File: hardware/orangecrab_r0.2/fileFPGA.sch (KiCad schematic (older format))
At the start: 11 parts, among them J6 JTAG, U3 ECP5U25, U6 AT25SF081

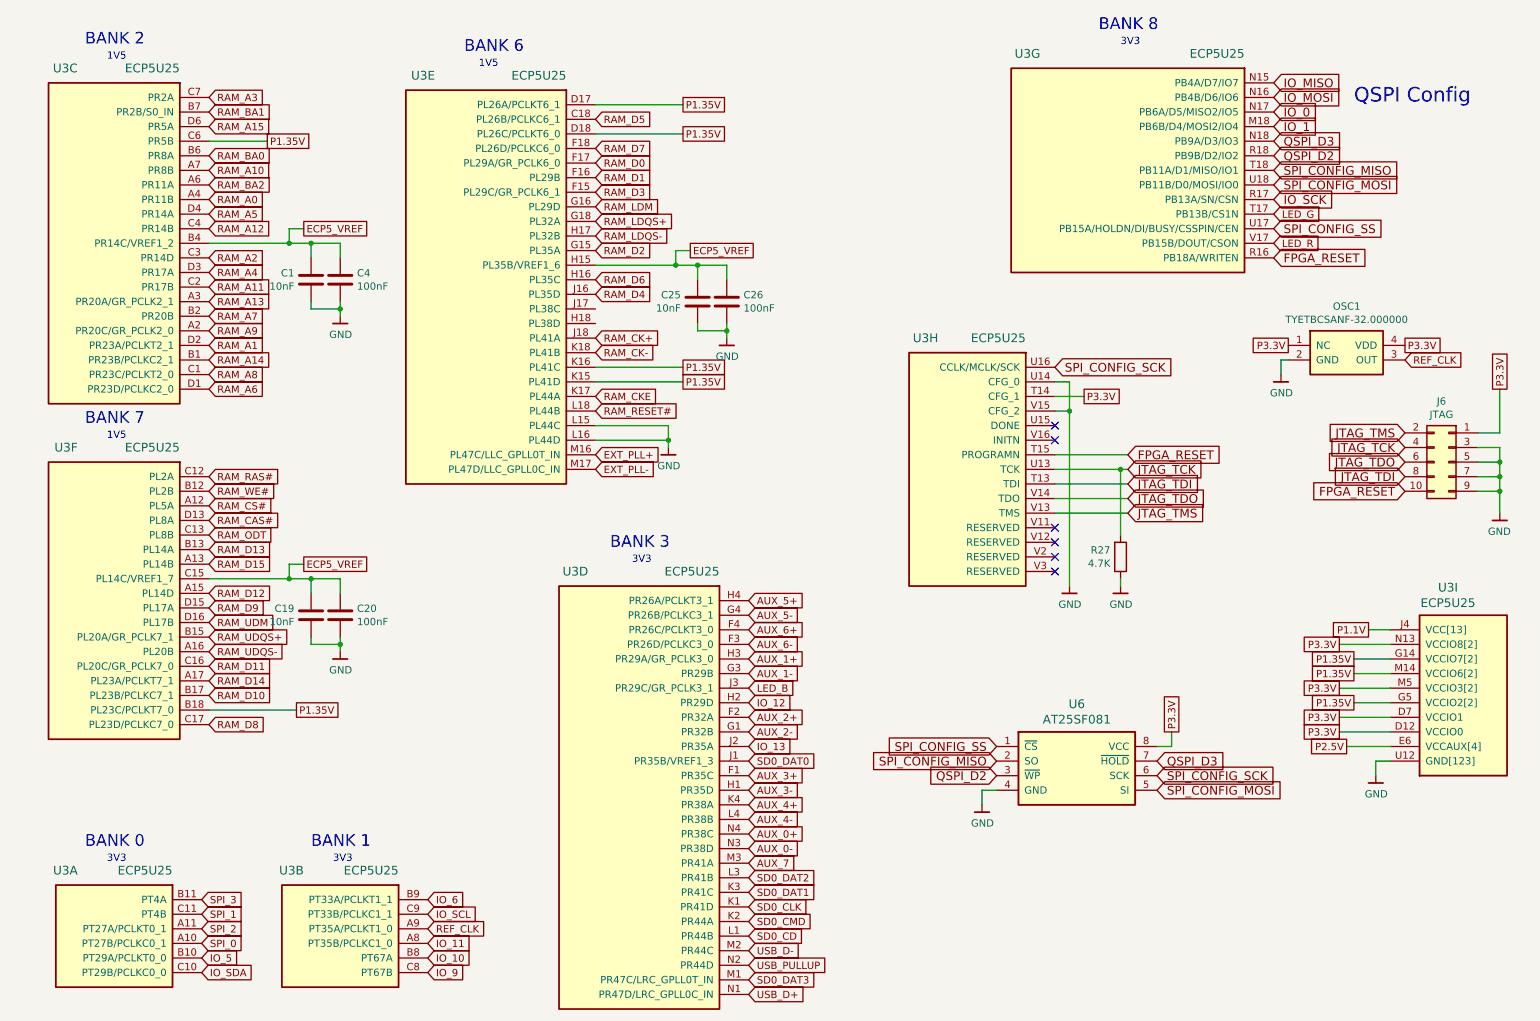
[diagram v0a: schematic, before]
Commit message: hw: Update I/O block routing new DDR3 signals.
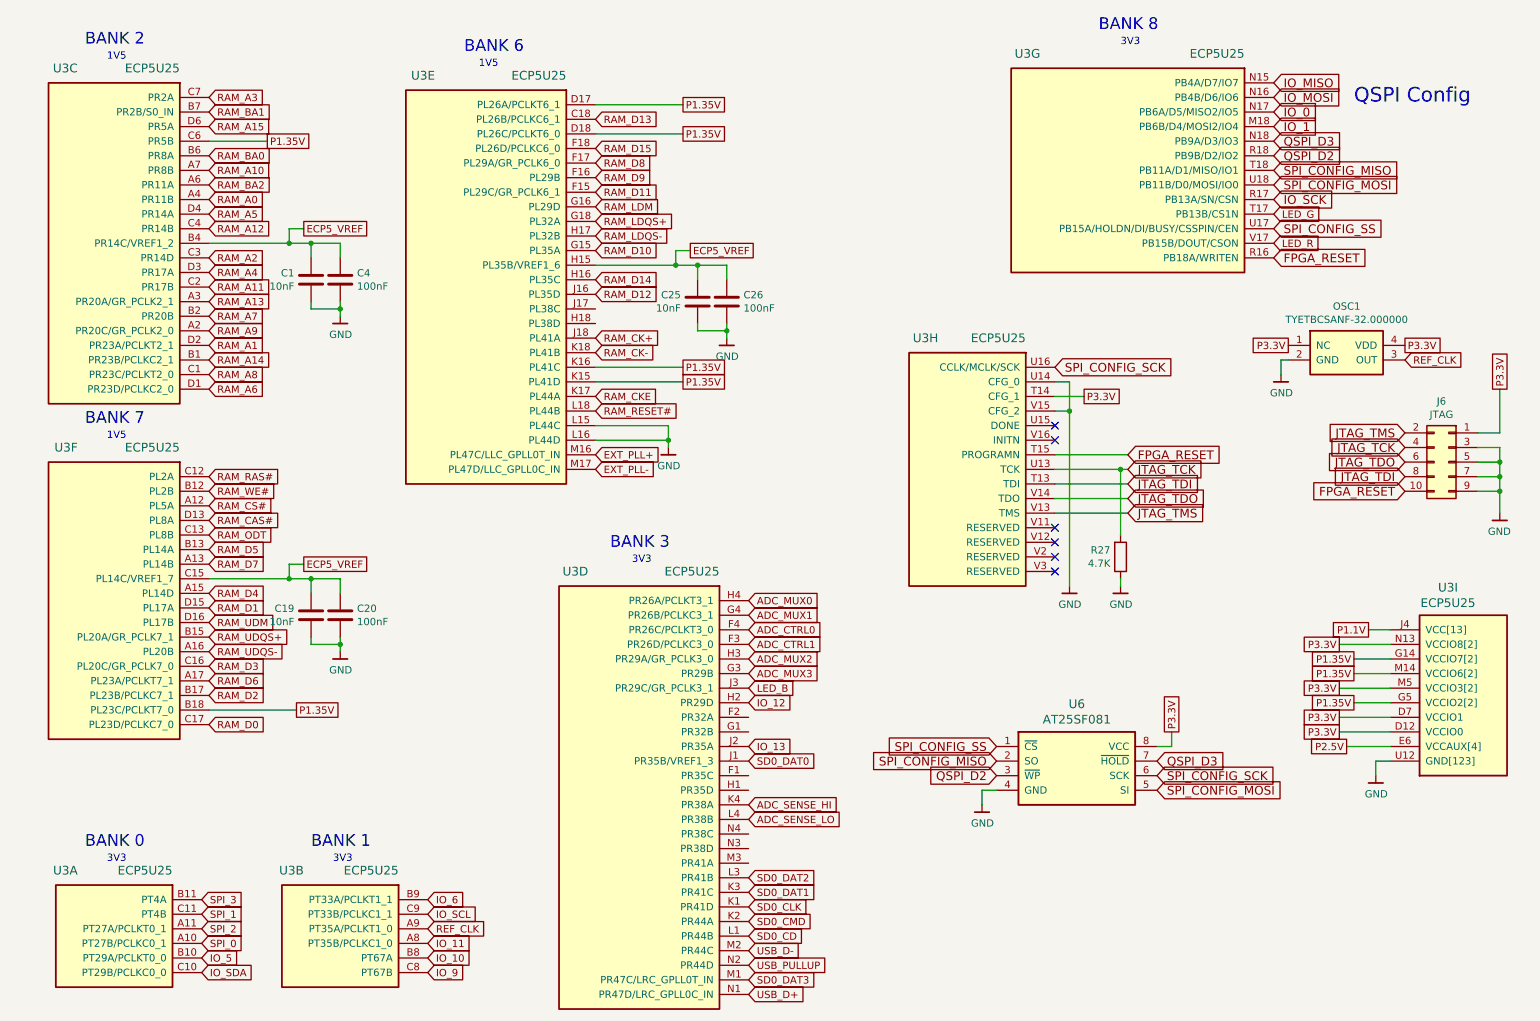
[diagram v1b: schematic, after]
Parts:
- U6: footprint gkl_housings_dfn:DFN-8-1EP_3x2mm_Pitch0.5mm -> Package_SON:WSON-8-1EP_6x5mm_P1.27mm_EP3.4x4mm
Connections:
- net RAM_D0: now also U3.C17 (PL23D/PCLKC7_0); no longer U3.F17 (PL29A/GR_PCLK6_0)
- net RAM_D1: now also U3.D15 (PL17A); no longer U3.F16 (PL29B)
- net RAM_D10: now also U3.G15 (PL35A); no longer U3.B17 (PL23B/PCLKC7_1)
- net RAM_D11: now also U3.F15 (PL29C/GR_PCLK6_1); no longer U3.C16 (PL20C/GR_PCLK7_0)
- net RAM_D12: now also U3.J16 (PL35D); no longer U3.A15 (PL14D)
- net RAM_D13: now also U3.C18 (PL26B/PCLKC6_1); no longer U3.B13 (PL14A)
- net RAM_D14: now also U3.H16 (PL35C); no longer U3.A17 (PL23A/PCLKT7_1)
- net RAM_D15: now also U3.F18 (PL26D/PCLKC6_0); no longer U3.A13 (PL14B)
- net RAM_D2: now also U3.B17 (PL23B/PCLKC7_1); no longer U3.G15 (PL35A)
- net RAM_D3: now also U3.C16 (PL20C/GR_PCLK7_0); no longer U3.F15 (PL29C/GR_PCLK6_1)
- net RAM_D4: now also U3.A15 (PL14D); no longer U3.J16 (PL35D)
- net RAM_D5: now also U3.B13 (PL14A); no longer U3.C18 (PL26B/PCLKC6_1)
- net RAM_D6: now also U3.A17 (PL23A/PCLKT7_1); no longer U3.H16 (PL35C)
- net RAM_D7: now also U3.A13 (PL14B); no longer U3.F18 (PL26D/PCLKC6_0)
- net RAM_D8: now also U3.F17 (PL29A/GR_PCLK6_0); no longer U3.C17 (PL23D/PCLKC7_0)
- net RAM_D9: now also U3.F16 (PL29B); no longer U3.D15 (PL17A)
- net AUX_0+: no longer names the net of U3.N4 (PR38C)
- net AUX_0-: no longer names the net of U3.N3 (PR38D)
- net AUX_1+ renamed ADC_MUX2
- net AUX_1- renamed ADC_MUX3
- net AUX_2+: no longer names the net of U3.F2 (PR32A)
- net AUX_2-: no longer names the net of U3.G1 (PR32B)
- net AUX_3+: no longer names the net of U3.F1 (PR35C)
- net AUX_3-: no longer names the net of U3.H1 (PR35D)
- net AUX_4+ renamed ADC_SENSE_HI
- net AUX_4- renamed ADC_SENSE_LO
- net AUX_5+ renamed ADC_MUX0
- net AUX_5- renamed ADC_MUX1
- net AUX_6+ renamed ADC_CTRL0
- net AUX_6- renamed ADC_CTRL1
- net AUX_7: no longer names the net of U3.M3 (PR41A)
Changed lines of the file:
@@
 NoConn ~ 7800 4500
 Text GLabel 4650 1700 2    50   Input ~ 0
+RAM_D8
+Text GLabel 4650 1800 2    50   Input ~ 0
+RAM_D9
+Text GLabel 4650 2300 2    50   Input ~ 0
+RAM_D10
+Text GLabel 4650 1900 2    50   Input ~ 0
+RAM_D11
+Text GLabel 4650 2600 2    50   Input ~ 0
+RAM_D12
+Text GLabel 4650 1400 2    50   Input ~ 0
+RAM_D13
+Text GLabel 4650 2500 2    50   Input ~ 0
+RAM_D14
+Text GLabel 4650 1600 2    50   Input ~ 0
+RAM_D15
+Text GLabel 2000 5550 2    50   Input ~ 0
 RAM_D0
-Text GLabel 4650 1800 2    50   Input ~ 0
+Text GLabel 2000 4750 2    50   Input ~ 0
 RAM_D1
-Text GLabel 4650 2300 2    50   Input ~ 0
+Text GLabel 2000 5350 2    50   Input ~ 0
 RAM_D2
-Text GLabel 4650 1900 2    50   Input ~ 0
+Text GLabel 2000 5150 2    50   Input ~ 0
 RAM_D3
-Text GLabel 4650 2600 2    50   Input ~ 0
+Text GLabel 2000 4650 2    50   Input ~ 0
 RAM_D4
-Text GLabel 4650 1400 2    50   Input ~ 0
+Text GLabel 2000 4350 2    50   Input ~ 0
 RAM_D5
-Text GLabel 4650 2500 2    50   Input ~ 0
+Text GLabel 2000 5250 2    50   Input ~ 0
 RAM_D6
-Text GLabel 4650 1600 2    50   Input ~ 0
+Text GLabel 2000 4450 2    50   Input ~ 0
 RAM_D7
-Text GLabel 2000 5550 2    50   Input ~ 0
-RAM_D8
-Text GLabel 2000 4750 2    50   Input ~ 0
-RAM_D9
-Text GLabel 2000 5350 2    50   Input ~ 0
-RAM_D10
-Text GLabel 2000 5150 2    50   Input ~ 0
-RAM_D11
-Text GLabel 2000 4650 2    50   Input ~ 0
-RAM_D12
-Text GLabel 2000 4350 2    50   Input ~ 0
-RAM_D13
-Text GLabel 2000 5250 2    50   Input ~ 0
-RAM_D14
-Text GLabel 2000 4450 2    50   Input ~ 0
-RAM_D15
 Text GLabel 2000 1950 2    50   Input ~ 0
 RAM_A0
@@
 Text GLabel 5700 5400 2    50   Input ~ 0
 IO_12
-Text GLabel 5700 6500 2    50   Input ~ 0
-AUX_7
 Text GLabel 5700 7100 2    50   Input ~ 0
 USB_D-
@@
 F 0 "U6" H 7950 6291 60  0000 C CNN
 F 1 "AT25SF081" H 7950 6185 60  0000 C CNN
-F 2 "gkl_housings_dfn:DFN-8-1EP_3x2mm_Pitch0.5mm" H 7950 6300 60  0001 C CNN
+F 2 "Package_SON:WSON-8-1EP_6x5mm_P1.27mm_EP3.4x4mm" H 7950 6300 60  0001 C CNN
 F 3 "" H 7950 6300 60  0001 C CNN
 F 4 "1265-1275-1-ND" H 3800 1900 50  0001 C CNN "SN-DK"
@@
 NoConn ~ 7800 3600
 NoConn ~ 7800 3500
-Text GLabel 5700 4900 2    50   Input ~ 0
-AUX_6+
-Text GLabel 5700 5000 2    50   Input ~ 0
-AUX_6-
-Text GLabel 5700 5900 2    50   Input ~ 0
-AUX_3+
-Text GLabel 5700 6000 2    50   Input ~ 0
-AUX_3-
-Text GLabel 5700 6300 2    50   Input ~ 0
-AUX_0+
-Text GLabel 5700 6400 2    50   Input ~ 0
-AUX_0-
-Text GLabel 5700 5100 2    50   Input ~ 0
-AUX_1+
-Text GLabel 5700 5200 2    50   Input ~ 0
-AUX_1-
-Text GLabel 5700 5500 2    50   Input ~ 0
-AUX_2+
-Text GLabel 5700 5600 2    50   Input ~ 0
-AUX_2-
-Text GLabel 5700 4700 2    50   Input ~ 0
-AUX_5+
-Text GLabel 5700 4800 2    50   Input ~ 0
-AUX_5-
-Text GLabel 5700 6100 2    50   Input ~ 0
-AUX_4+
-Text GLabel 5700 6200 2    50   Input ~ 0
-AUX_4-
 Text GLabel 2000 1650 2    50   Input ~ 0
 RAM_BA0
@@
 Text GLabel 2000 1450 2    50   Input ~ 0
 RAM_A15
+Text GLabel 5700 4700 2    50   Input ~ 0
+ADC_MUX0
+Text GLabel 5700 4800 2    50   Input ~ 0
+ADC_MUX1
+Text GLabel 5700 5100 2    50   Input ~ 0
+ADC_MUX2
+Text GLabel 5700 5200 2    50   Input ~ 0
+ADC_MUX3
+Text GLabel 5700 5000 2    50   Input ~ 0
+ADC_CTRL1
+Text GLabel 5700 6200 2    50   Input ~ 0
+ADC_SENSE_LO
+Text GLabel 5700 6100 2    50   Input ~ 0
+ADC_SENSE_HI
+Text GLabel 5700 4900 2    50   Input ~ 0
+ADC_CTRL0
 $EndSCHEMATC

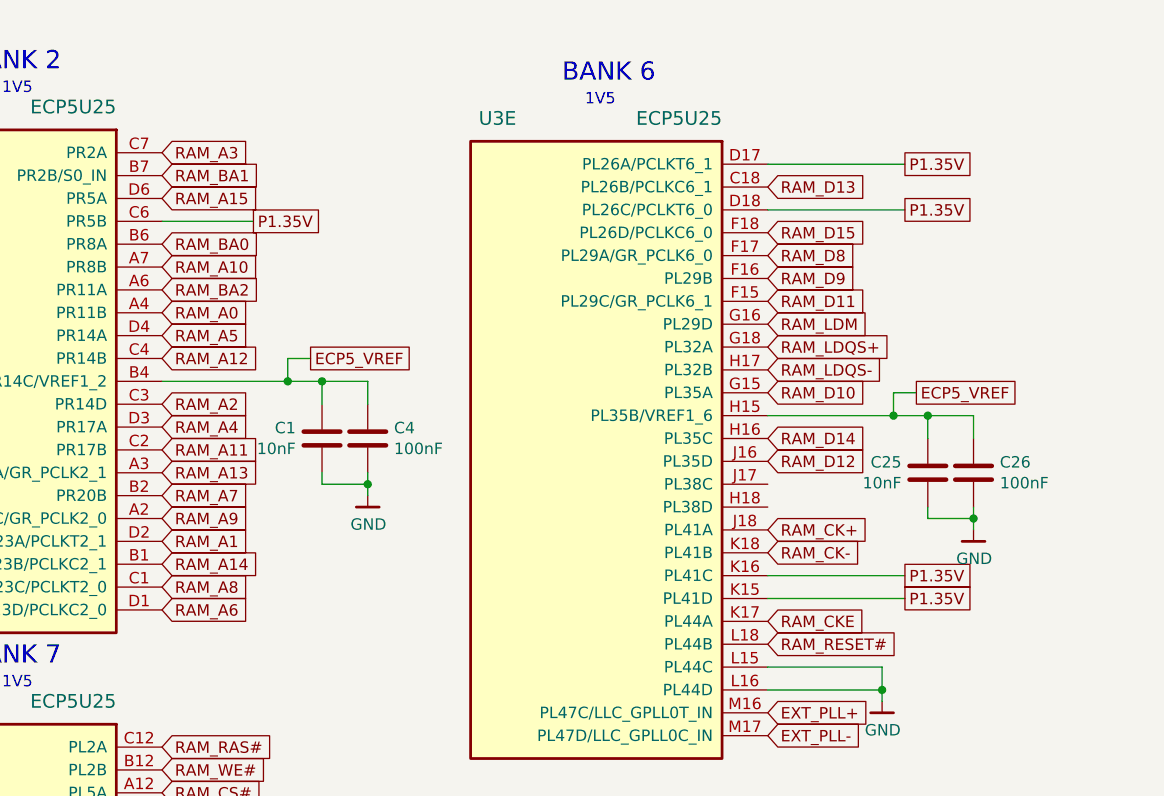
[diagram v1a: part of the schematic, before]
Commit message: hw: update DDR3 signals
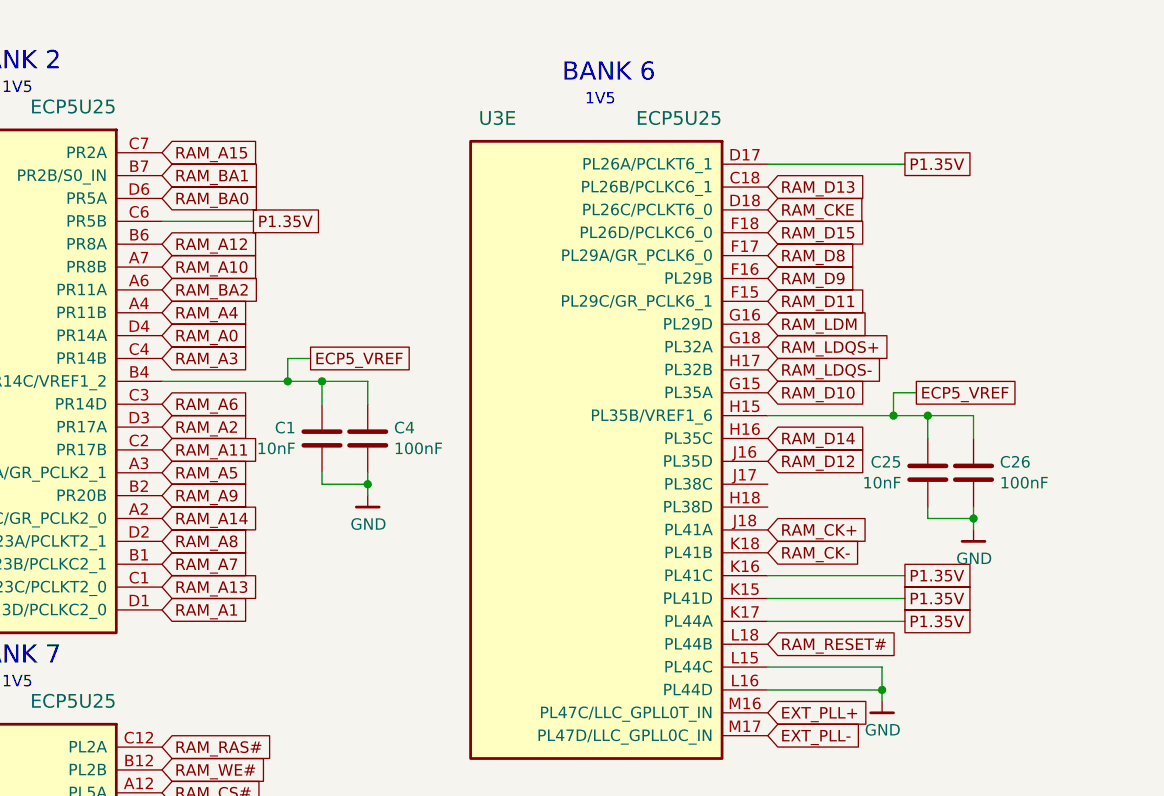
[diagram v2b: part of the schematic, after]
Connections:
- net P1.35V: now also U3.K17 (PL44A); no longer U3.D18 (PL26C/PCLKT6_0)
- net RAM_A0: now also U3.D4 (PR14A); no longer U3.A4 (PR11B)
- net RAM_A1: now also U3.D1 (PR23D/PCLKC2_0); no longer U3.D2 (PR23A/PCLKT2_1)
- net RAM_A12: now also U3.B6 (PR8A); no longer U3.C4 (PR14B)
- net RAM_A13: now also U3.C1 (PR23C/PCLKT2_0); no longer U3.A3 (PR20A/GR_PCLK2_1)
- net RAM_A14: now also U3.A2 (PR20C/GR_PCLK2_0); no longer U3.B1 (PR23B/PCLKC2_1)
- net RAM_A15: now also U3.C7 (PR2A); no longer U3.D6 (PR5A)
- net RAM_A2: now also U3.D3 (PR17A); no longer U3.C3 (PR14D)
- net RAM_A3: now also U3.C4 (PR14B); no longer U3.C7 (PR2A)
- net RAM_A4: now also U3.A4 (PR11B); no longer U3.D3 (PR17A)
- net RAM_A5: now also U3.A3 (PR20A/GR_PCLK2_1); no longer U3.D4 (PR14A)
- net RAM_A6: now also U3.C3 (PR14D); no longer U3.D1 (PR23D/PCLKC2_0)
- net RAM_A7: now also U3.B1 (PR23B/PCLKC2_1); no longer U3.B2 (PR20B)
- net RAM_A8: now also U3.D2 (PR23A/PCLKT2_1); no longer U3.C1 (PR23C/PCLKT2_0)
- net RAM_A9: now also U3.B2 (PR20B); no longer U3.A2 (PR20C/GR_PCLK2_0)
- net RAM_BA0: now also U3.D6 (PR5A); no longer U3.B6 (PR8A)
- net RAM_CKE: now also U3.D18 (PL26C/PCLKT6_0); no longer U3.K17 (PL44A)
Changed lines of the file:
@@
 Text GLabel 2000 4450 2    50   Input ~ 0
 RAM_D7
+Text GLabel 2000 2050 2    50   Input ~ 0
+RAM_A0
+Text GLabel 2000 3250 2    50   Input ~ 0
+RAM_A1
+Text GLabel 2000 2450 2    50   Input ~ 0
+RAM_A2
+Text GLabel 2000 2150 2    50   Input ~ 0
+RAM_A3
 Text GLabel 2000 1950 2    50   Input ~ 0
-RAM_A0
+RAM_A4
+Text GLabel 2000 2650 2    50   Input ~ 0
+RAM_A5
+Text GLabel 2000 2350 2    50   Input ~ 0
+RAM_A6
+Text GLabel 2000 3050 2    50   Input ~ 0
+RAM_A7
 Text GLabel 2000 2950 2    50   Input ~ 0
-RAM_A1
-Text GLabel 2000 2350 2    50   Input ~ 0
-RAM_A2
-Text GLabel 2000 1250 2    50   Input ~ 0
-RAM_A3
-Text GLabel 2000 2450 2    50   Input ~ 0
-RAM_A4
-Text GLabel 2000 2050 2    50   Input ~ 0
-RAM_A5
-Text GLabel 2000 3250 2    50   Input ~ 0
-RAM_A6
-Text GLabel 2000 2750 2    50   Input ~ 0
-RAM_A7
-Text GLabel 2000 3150 2    50   Input ~ 0
 RAM_A8
 Text GLabel 2000 1750 2    50   Input ~ 0
@@
 Text GLabel 2000 2550 2    50   Input ~ 0
 RAM_A11
-Text GLabel 2000 2150 2    50   Input ~ 0
+Text GLabel 2000 1650 2    50   Input ~ 0
 RAM_A12
 Text GLabel 4650 2100 2    50   Input ~ 0
@@
 Wire Wire Line
 	2900 2700 2900 2750
-Text GLabel 2600 5450 2    50   UnSpc ~ 0
-P1.35V
-Wire Wire Line
-	2600 5450 2000 5450
-Text GLabel 2000 2850 2    50   Input ~ 0
+Text GLabel 5250 3300 2    50   UnSpc ~ 0
+P1.35V
+Wire Wire Line
+	5250 3300 4650 3300
+Text GLabel 2000 2750 2    50   Input ~ 0
 RAM_A9
 Text GLabel 2400 1550 2    50   UnSpc ~ 0
@@
 Wire Wire Line
 	10100 5200 9850 5200
-Text GLabel 4650 3300 2    50   Input ~ 0
+Text GLabel 4650 1500 2    50   Input ~ 0
 RAM_CKE
 Text GLabel 2000 3950 2    50   Input ~ 0
@@
 Text GLabel 8000 3300 2    50   UnSpc ~ 0
 P3.3V
-Text GLabel 5250 1500 2    50   UnSpc ~ 0
-P1.35V
-Wire Wire Line
-	5250 1500 4650 1500
+Text GLabel 2600 5450 2    50   UnSpc ~ 0
+P1.35V
+Wire Wire Line
+	2600 5450 2000 5450
 Text GLabel 5250 3100 2    50   UnSpc ~ 0
 P1.35V
@@
 NoConn ~ 7800 3600
 NoConn ~ 7800 3500
-Text GLabel 2000 1650 2    50   Input ~ 0
+Text GLabel 2000 1450 2    50   Input ~ 0
 RAM_BA0
 Text GLabel 2000 1850 2    50   Input ~ 0
@@
 Text GLabel 4650 3400 2    50   Input ~ 0
 RAM_RESET#
-Text GLabel 2000 2650 2    50   Input ~ 0
+Text GLabel 2000 3150 2    50   Input ~ 0
 RAM_A13
-Text GLabel 2000 3050 2    50   Input ~ 0
+Text GLabel 2000 2850 2    50   Input ~ 0
 RAM_A14
-Text GLabel 2000 1450 2    50   Input ~ 0
+Text GLabel 2000 1250 2    50   Input ~ 0
 RAM_A15
 Text GLabel 5700 4700 2    50   Input ~ 0

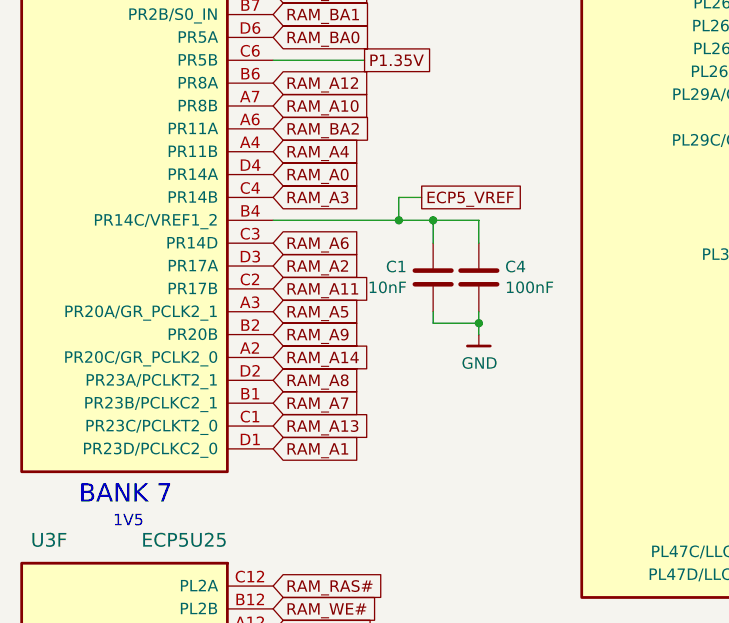
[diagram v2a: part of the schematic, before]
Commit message: hw: Completed first pass of new DD3 routing.
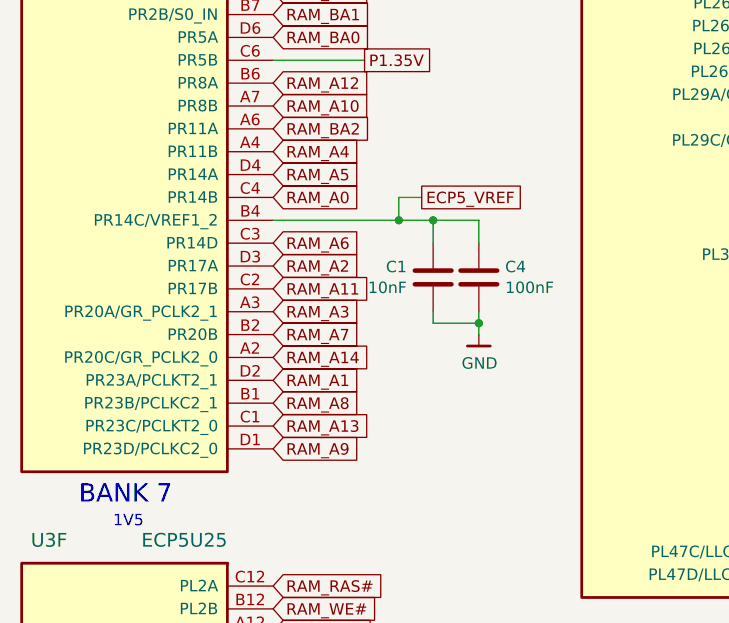
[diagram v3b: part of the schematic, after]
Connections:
- net RAM_A0: now also U3.C4 (PR14B); no longer U3.D4 (PR14A)
- net RAM_A1: now also U3.D2 (PR23A/PCLKT2_1); no longer U3.D1 (PR23D/PCLKC2_0)
- net RAM_A3: now also U3.A3 (PR20A/GR_PCLK2_1); no longer U3.C4 (PR14B)
- net RAM_A5: now also U3.D4 (PR14A); no longer U3.A3 (PR20A/GR_PCLK2_1)
- net RAM_A7: now also U3.B2 (PR20B); no longer U3.B1 (PR23B/PCLKC2_1)
- net RAM_A8: now also U3.B1 (PR23B/PCLKC2_1); no longer U3.D2 (PR23A/PCLKT2_1)
- net RAM_A9: now also U3.D1 (PR23D/PCLKC2_0); no longer U3.B2 (PR20B)
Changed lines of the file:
@@
 Text GLabel 2000 4450 2    50   Input ~ 0
 RAM_D7
-Text GLabel 2000 2050 2    50   Input ~ 0
+Text GLabel 2000 2150 2    50   Input ~ 0
 RAM_A0
-Text GLabel 2000 3250 2    50   Input ~ 0
+Text GLabel 2000 2950 2    50   Input ~ 0
 RAM_A1
 Text GLabel 2000 2450 2    50   Input ~ 0
 RAM_A2
-Text GLabel 2000 2150 2    50   Input ~ 0
+Text GLabel 2000 2650 2    50   Input ~ 0
 RAM_A3
 Text GLabel 2000 1950 2    50   Input ~ 0
 RAM_A4
-Text GLabel 2000 2650 2    50   Input ~ 0
+Text GLabel 2000 2050 2    50   Input ~ 0
 RAM_A5
 Text GLabel 2000 2350 2    50   Input ~ 0
 RAM_A6
+Text GLabel 2000 2750 2    50   Input ~ 0
+RAM_A7
 Text GLabel 2000 3050 2    50   Input ~ 0
-RAM_A7
-Text GLabel 2000 2950 2    50   Input ~ 0
 RAM_A8
 Text GLabel 2000 1750 2    50   Input ~ 0
@@
 Wire Wire Line
 	5250 3300 4650 3300
-Text GLabel 2000 2750 2    50   Input ~ 0
+Text GLabel 2000 3250 2    50   Input ~ 0
 RAM_A9
 Text GLabel 2400 1550 2    50   UnSpc ~ 0
